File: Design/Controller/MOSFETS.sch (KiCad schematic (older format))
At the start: 60 parts, among them Q10 BSS127, Q11 BSS127, Q12 BSS127, Q13 BSS127, Q14 BSS127, Q15 BSS127, Q16 BSS127, Q17 BSS127, Q18 BSS127, Q19 BSS127, Q2 BSS127, Q20 BSS127, Q21 BSS127, Q22 BSS127, Q23 BSS127, Q24 BSS127, Q25 BSS127, Q26 BSS127, Q27 BSS127, Q28 BSS127, Q29 BSS127, Q3 BSS127, Q30 BSS127, Q31 BSS127, Q32 BSS127, Q33 BSS127, Q34 BSS127, Q35 BSS127, Q36 BSS127, Q37 BSS127, Q38 BSS127, Q39 BSS127, Q4 BSS127, Q40 BSS127, Q41 BSS127, Q42 BSS127, Q43 BSS127, Q44 BSS127, Q45 BSS127, Q46 BSS127, Q47 BSS127, Q48 BSS127, Q49 BSS127, Q5 BSS127, Q50 BSS127, Q51 BSS127, Q52 BSS127, Q53 BSS127, Q54 BSS127, Q55 BSS127, Q56 BSS127, Q57 BSS127, Q58 BSS127, Q59 BSS127, Q6 BSS127, Q60 BSS127, Q61 BSS127, Q7 BSS127, Q8 BSS127, Q9 BSS127

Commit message: Add part numbers to symbols in NixieController schematic for BOM
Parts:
- Q10, Q11, Q12, Q13, Q14, Q15, Q16, Q17, Q18, Q19, Q2, Q20, Q21, Q22, Q23, Q24, Q25, Q26, Q27, Q28, Q29, Q3, Q30, Q31, Q32, Q33, Q34, Q35, Q36, Q37, Q38, Q39, Q4, Q40, Q41, Q42, Q43, Q44, Q45, Q46, Q47, Q48, Q49, Q5, Q50, Q51, Q52, Q53, Q54, Q55, Q56, Q57, Q58, Q59, Q6, Q60, Q61, Q7, Q8, Q9: Digikey # (none) -> BSS127S-7DIDKR-ND; Manufacturer (none) -> DIODES

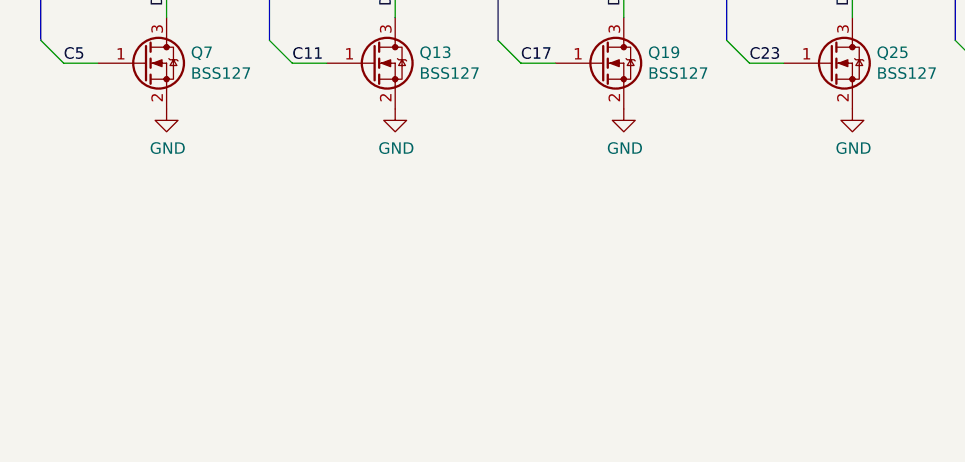
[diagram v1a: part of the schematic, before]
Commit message: Add license notice to all human readable files
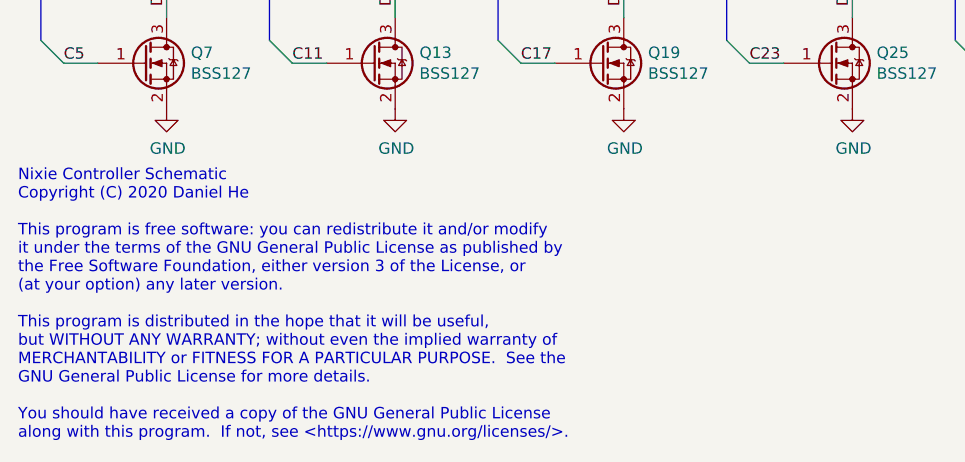
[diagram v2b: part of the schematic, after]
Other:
- note added: "Nixie Controller Schematic\nCopyright (C) 2020 Daniel He\n\nThis program is free software: you can redistribute it and/or modify\nit under the terms of the GNU General Public License as published by\nthe Free Software Foundation, either version 3 of the License, or\n(at your option) any later version.\n\nThis program is distributed in the hope that it will be useful,\nbut WITHOUT ANY WARRANTY; wi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"
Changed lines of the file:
@@
 Text HLabel 9650 850  1    50   Input ~ 0
 C[0..59]
+Text Notes 550  7700 0    50   ~ 0
+Nixie Controller Schematic\nCopyright (C) 2020 Daniel He\n\nThis program is free software: you can redistribute it and/or modify\nit under the terms of the GNU General Public License as published by\nthe Free Software Foundation, either version 3 of the License, or\n(at your option) any later version.\n\nThis program is distributed in the hope that it will be useful,\nbut WITHOUT ANY WARRANTY; without even the implied warranty of\nMERCHANTABILITY or FITNESS FOR A PARTICULAR PURPOSE.  See the\nGNU General Public License for more details.\n\nYou should have received a copy of the GNU General Public License\nalong with this program.  If not, see <https://www.gnu.org/licenses/>.
 Wire Bus Line
 	650  850  650  5950
